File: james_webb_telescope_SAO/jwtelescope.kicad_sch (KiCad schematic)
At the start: 1 part

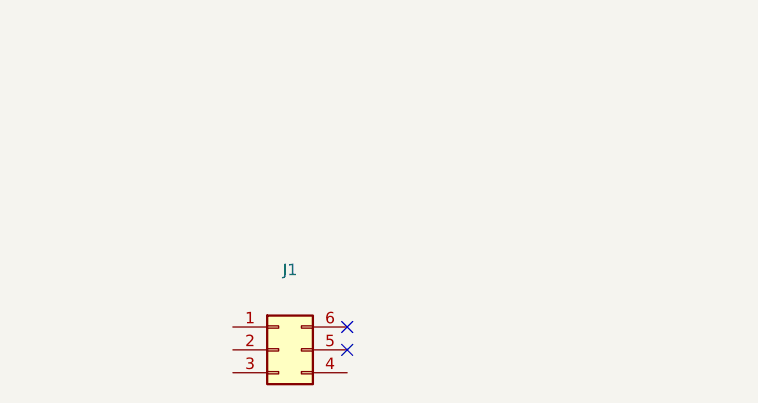
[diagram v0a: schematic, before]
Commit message: first attempt at a v2 of the JWT that includes LEDs
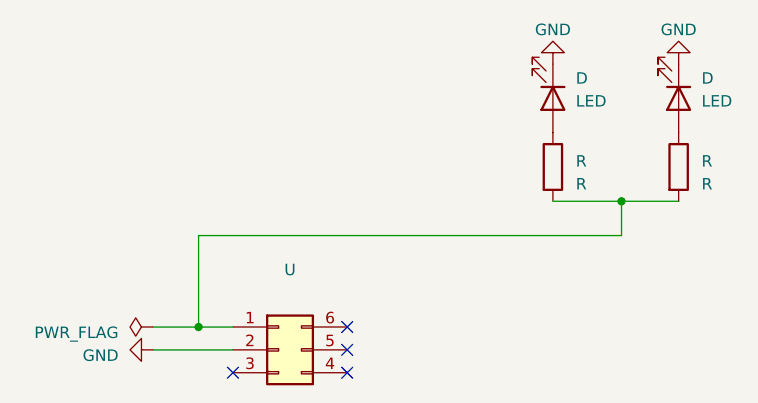
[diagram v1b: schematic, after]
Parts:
- added D (x2): LED, symbol Device:LED
- added R (x2): R, symbol Device:R
- renumbered J1 to U
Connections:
- net at U.1 (Pin_1): now also R.2, R.2
- net GND: now reaches U.2 (Pin_2)
- net GND: now also D.1 (K), D.1 (K)
- new net: D.2 (A), R.1 (x2)
- no-connect marks 2 -> 4
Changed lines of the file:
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@@
-(kicad_sch (version 20211123) (generator eeschema)
+(kicad_sch (version 20220404) (generator eeschema)
   (paper "A4")
+  (junction (at 101.6 82.55) (diameter 0) (color 0 0 0 0)
+  )
+  (junction (at 148.59 68.58) (diameter 0) (color 0 0 0 0)
+  )
+  (no_connect (at 118.11 82.55))
+  (no_connect (at 105.41 87.63))
+  (no_connect (at 118.11 87.63))
   (no_connect (at 118.11 85.09))
-  (no_connect (at 118.11 82.55))
+  (wire (pts (xy 148.59 68.58) (xy 154.94 68.58))
+    (stroke (width 0) (type default))
+  )
+  (wire (pts (xy 140.97 68.58) (xy 148.59 68.58))
+    (stroke (width 0) (type default))
+  )
+  (wire (pts (xy 101.6 72.39) (xy 101.6 82.55))
+    (stroke (width 0) (type default))
+  )
+  (wire (pts (xy 96.52 85.09) (xy 105.41 85.09))
+    (stroke (width 0) (type default))
+  )
+  (wire (pts (xy 101.6 82.55) (xy 105.41 82.55))
+    (stroke (width 0) (type default))
+  )
+  (wire (pts (xy 148.59 68.58) (xy 148.59 72.39))
+    (stroke (width 0) (type default))
+  )
+  (wire (pts (xy 148.59 72.39) (xy 101.6 72.39))
+    (stroke (width 0) (type default))
+  )
+  (wire (pts (xy 96.52 82.55) (xy 101.6 82.55))
+    (stroke (width 0) (type default))
+  )
+  (symbol (lib_id "power:GND") (at 96.52 85.09 270) (unit 1)
+    (in_bom yes) (on_board yes) (fields_autoplaced)
+    (default_instance (reference "#PWR") (unit 1) (value "GND") (footprint ""))
+    (property "Reference" "#PWR" (id 0) (at 90.17 85.09 0)
+      (effects (font (size 1.27 1.27)) hide)
+    )
+    (property "Value" "GND" (id 1) (at 92.71 85.725 90)
+      (effects (font (size 1.27 1.27)) (justify right))
+    )
+    (property "Footprint" "" (id 2) (at 96.52 85.09 0)
+      (effects (font (size 1.27 1.27)) hide)
+    )
+    (property "Datasheet" "" (id 3) (at 96.52 85.09 0)
+      (effects (font (size 1.27 1.27)) hide)
+    )
+    (pin "1")
+  )
+  (symbol (lib_id "Device:LED") (at 154.94 57.15 270) (unit 1)
+    (in_bom yes) (on_board yes) (fields_autoplaced)
+    (default_instance (reference "D") (unit 1) (value "LED") (footprint ""))
+    (property "Reference" "D" (id 0) (at 157.48 54.9275 90)
+      (effects (font (size 1.27 1.27)) (justify left))
+    )
+    (property "Value" "LED" (id 1) (at 157.48 57.4675 90)
+      (effects (font (size 1.27 1.27)) (justify left))
+    )
+    (property "Footprint" "" (id 2) (at 154.94 57.15 0)
+      (effects (font (size 1.27 1.27)) hide)
+    )
+    (property "Datasheet" "~" (id 3) (at 154.94 57.15 0)
+      (effects (font (size 1.27 1.27)) hide)
+    )
+    (pin "1")
+    (pin "2")
+  )
+  (symbol (lib_id "power:GND") (at 140.97 53.34 180) (unit 1)
+    (in_bom yes) (on_board yes) (fields_autoplaced)
+    (default_instance (reference "#PWR") (unit 1) (value "GND") (footprint ""))
+    (property "Reference" "#PWR" (id 0) (at 140.97 46.99 0)
+      (effects (font (size 1.27 1.27)) hide)
+    )
+    (property "Value" "GND" (id 1) (at 140.97 49.53 0)
+      (effects (font (size 1.27 1.27)))
+    )
+    (property "Footprint" "" (id 2) (at 140.97 53.34 0)
+      (effects (font (size 1.27 1.27)) hide)
+    )
+    (property "Datasheet" "" (id 3) (at 140.97 53.34 0)
+      (effects (font (size 1.27 1.27)) hide)
+    )
+    (pin "1")
+  )
+  (symbol (lib_id "Device:R") (at 154.94 64.77 0) (unit 1)
+    (in_bom yes) (on_board yes) (fields_autoplaced)
+    (default_instance (reference "R") (unit 1) (value "R") (footprint ""))
+    (property "Reference" "R" (id 0) (at 157.48 64.135 0)
+      (effects (font (size 1.27 1.27)) (justify left))
+    )
+    (property "Value" "R" (id 1) (at 157.48 66.675 0)
+      (effects (font (size 1.27 1.27)) (justify left))
+    )
+    (property "Footprint" "" (id 2) (at 153.162 64.77 90)
+      (effects (font (size 1.27 1.27)) hide)
+    )
+    (property "Datasheet" "~" (id 3) (at 154.94 64.77 0)
+      (effects (font (size 1.27 1.27)) hide)
+    )
+    (pin "1")
+    (pin "2")
+  )
+  (symbol (lib_id "power:GND") (at 154.94 53.34 180) (unit 1)
+    (in_bom yes) (on_board yes) (fields_autoplaced)
+    (default_instance (reference "#PWR") (unit 1) (value "GND") (footprint ""))
+    (property "Reference" "#PWR" (id 0) (at 154.94 46.99 0)
+      (effects (font (size 1.27 1.27)) hide)
+    )
+    (property "Value" "GND" (id 1) (at 154.94 49.53 0)
+      (effects (font (size 1.27 1.27)))
+    )
+    (property "Footprint" "" (id 2) (at 154.94 53.34 0)
+      (effects (font (size 1.27 1.27)) hide)
+    )
+    (property "Datasheet" "" (id 3) (at 154.94 53.34 0)
+      (effects (font (size 1.27 1.27)) hide)
+    )
+    (pin "1")
+  )
+  (symbol (lib_id "Device:LED") (at 140.97 57.15 270) (unit 1)
+    (in_bom yes) (on_board yes) (fields_autoplaced)
+    (default_instance (reference "D") (unit 1) (value "LED") (footprint ""))
+    (property "Reference" "D" (id 0) (at 143.51 54.9275 90)
+      (effects (font (size 1.27 1.27)) (justify left))
+    )
+    (property "Value" "LED" (id 1) (at 143.51 57.4675 90)
+      (effects (font (size 1.27 1.27)) (justify left))
+    )
+    (property "Footprint" "" (id 2) (at 140.97 57.15 0)
+      (effects (font (size 1.27 1.27)) hide)
+    )
+    (property "Datasheet" "~" (id 3) (at 140.97 57.15 0)
+      (effects (font (size 1.27 1.27)) hide)
+    )
+    (pin "1")
+    (pin "2")
+  )
   (symbol (lib_id "Connector_Generic:Conn_02x03_Counter_Clockwise") (at 110.49 85.09 0) (unit 1)
     (in_bom yes) (on_board yes) (fields_autoplaced)
-    (property "Reference" "J1" (id 0) (at 111.76 76.2 0))
-    (property "Value" "" (id 1) (at 111.76 78.74 0))
+    (default_instance (reference "U") (unit 1) (value "") (footprint ""))
+    (property "Reference" "U" (id 0) (at 111.76 76.2 0)
+      (effects (font (size 1.27 1.27)))
+    )
+    (property "Value" "" (id 1) (at 111.76 78.74 0)
+      (effects (font (size 1.27 1.27)))
+    )
     (property "Footprint" "" (id 2) (at 110.49 85.09 0)
       (effects (font (size 1.27 1.27)) hide)
@@
     (pin "6")
   )
+  (symbol (lib_id "power:PWR_FLAG") (at 96.52 82.55 90) (unit 1)
+    (in_bom yes) (on_board yes) (fields_autoplaced)
+    (default_instance (reference "#FLG") (unit 1) (value "PWR_FLAG") (footprint ""))
+    (property "Reference" "#FLG" (id 0) (at 94.615 82.55 0)
+      (effects (font (size 1.27 1.27)) hide)
+    )
+    (property "Value" "PWR_FLAG" (id 1) (at 92.71 83.185 90)
+      (effects (font (size 1.27 1.27)) (justify left))
+    )
+    (property "Footprint" "" (id 2) (at 96.52 82.55 0)
+      (effects (font (size 1.27 1.27)) hide)
+    )
+    (property "Datasheet" "~" (id 3) (at 96.52 82.55 0)
+      (effects (font (size 1.27 1.27)) hide)
+    )
+    (pin "1")
+  )
+  (symbol (lib_id "Device:R") (at 140.97 64.77 0) (unit 1)
+    (in_bom yes) (on_board yes) (fields_autoplaced)
+    (default_instance (reference "R") (unit 1) (value "R") (footprint ""))
+    (property "Reference" "R" (id 0) (at 143.51 64.135 0)
+      (effects (font (size 1.27 1.27)) (justify left))
+    )
+    (property "Value" "R" (id 1) (at 143.51 66.675 0)
+      (effects (font (size 1.27 1.27)) (justify left))
+    )
+    (property "Footprint" "" (id 2) (at 139.192 64.77 90)
+      (effects (font (size 1.27 1.27)) hide)
+    )
+    (property "Datasheet" "~" (id 3) (at 140.97 64.77 0)
+      (effects (font (size 1.27 1.27)) hide)
+    )
+    (pin "1")
+    (pin "2")
+  )
   (sheet_instances
     (path "/" (page "1"))
   )
   (symbol_instances
+    (path "/d874f68c-607f-4a54-a6d5-a48ba6f1182d"
+      (reference "#FLG02") (unit 1) (value "PWR_FLAG") (footprint "")
+    )
+    (path "/0abb490e-3fb7-4bb4-a31b-23947b902014"
+      (reference "#PWR02") (unit 1) (value "GND") (footprint "")
+    )
+    (path "/649c805a-a28f-485c-af2a-bebbac8110cb"
+      (reference "#PWR03") (unit 1) (value "GND") (footprint "")
+    )
+    (path "/a1318bb4-2012-4d4a-ba2a-42b0d3b3aeab"
+      (reference "#PWR04") (unit 1) (value "GND") (footprint "")
+    )
+    (path "/b376f188-0907-42c6-817e-ebf9d49a58bb"
+      (reference "D1") (unit 1) (value "LED") (footprint "")
+    )
+    (path "/57d8d705-f080-4eb9-a04f-8255ecb8d445"
+      (reference "D2") (unit 1) (value "LED") (footprint "")
+    )
     (path "/bd0fc8ee-c22d-4133-8e6a-9fdd47c9d8c1"
       (reference "J1") (unit 1) (value "Conn_02x03_Counter_Clockwise") (footprint "Connector_PinSocket_2.54mm:PinSocket_2x03_P2.54mm_Vertical")
     )
-  )
+    (path "/e0e80cb0-808c-4d1e-88b5-53b85dedaf04"
+      (reference "R1") (unit 1) (value "R") (footprint "")
+    )
+    (path "/95eed00c-e8d4-437d-a0b2-c05cbcc6ece7"
+      (reference "R2") (unit 1) (value "R") (footprint "")
+    )
+  )
